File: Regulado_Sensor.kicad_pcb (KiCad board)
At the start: 2 copper layers, 57 parts

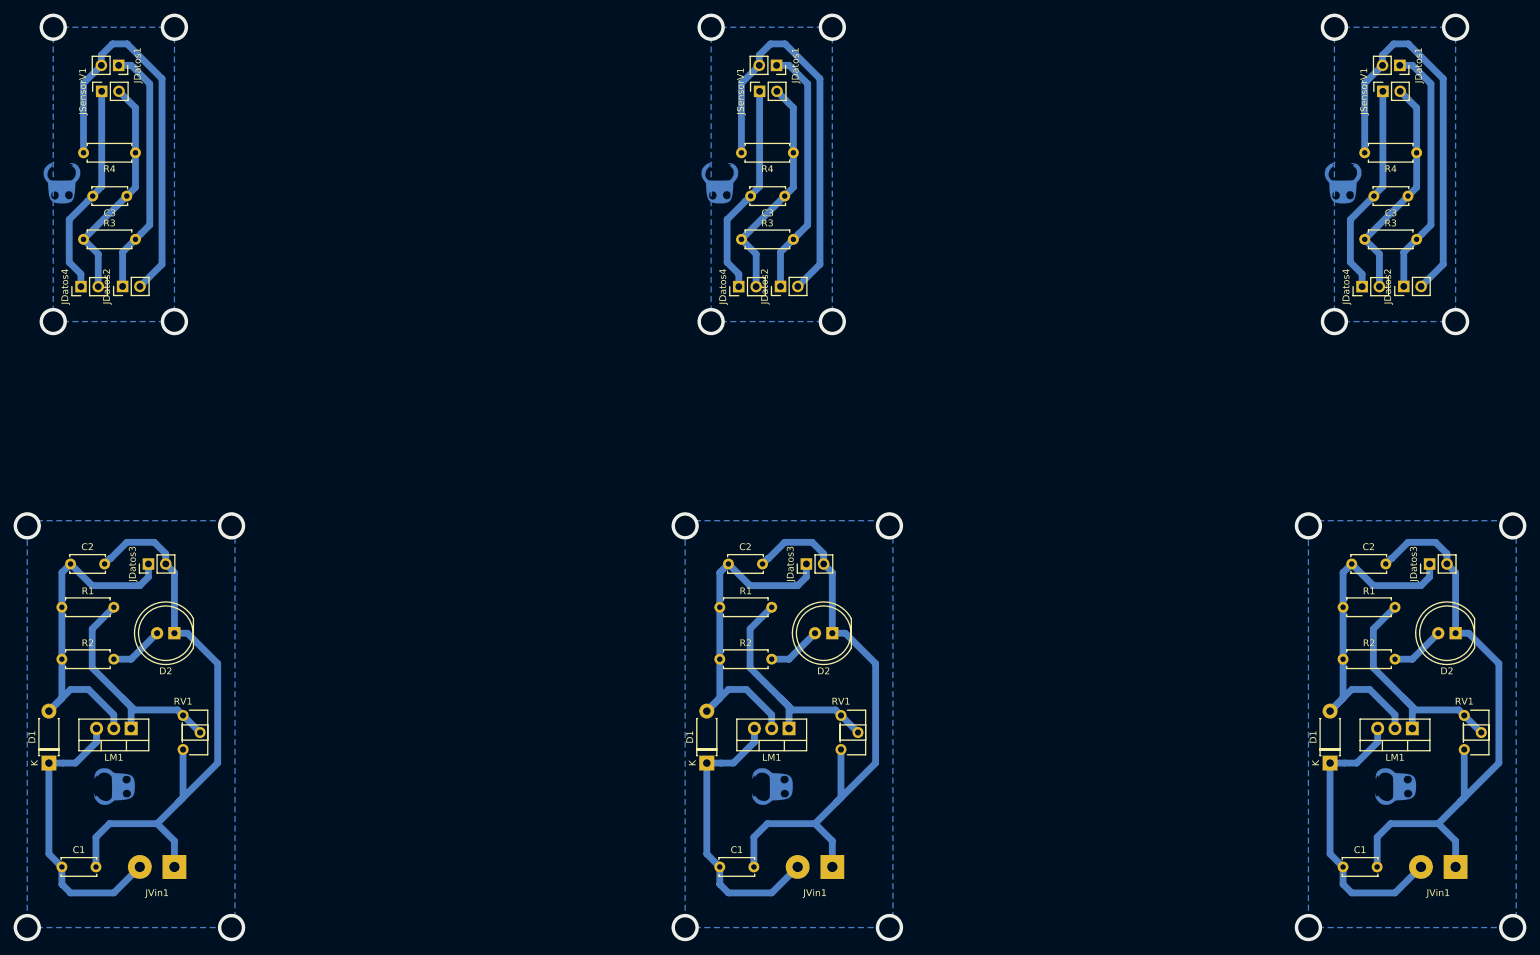
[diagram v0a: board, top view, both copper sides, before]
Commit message: Se arreglo un error en la placa de I2C
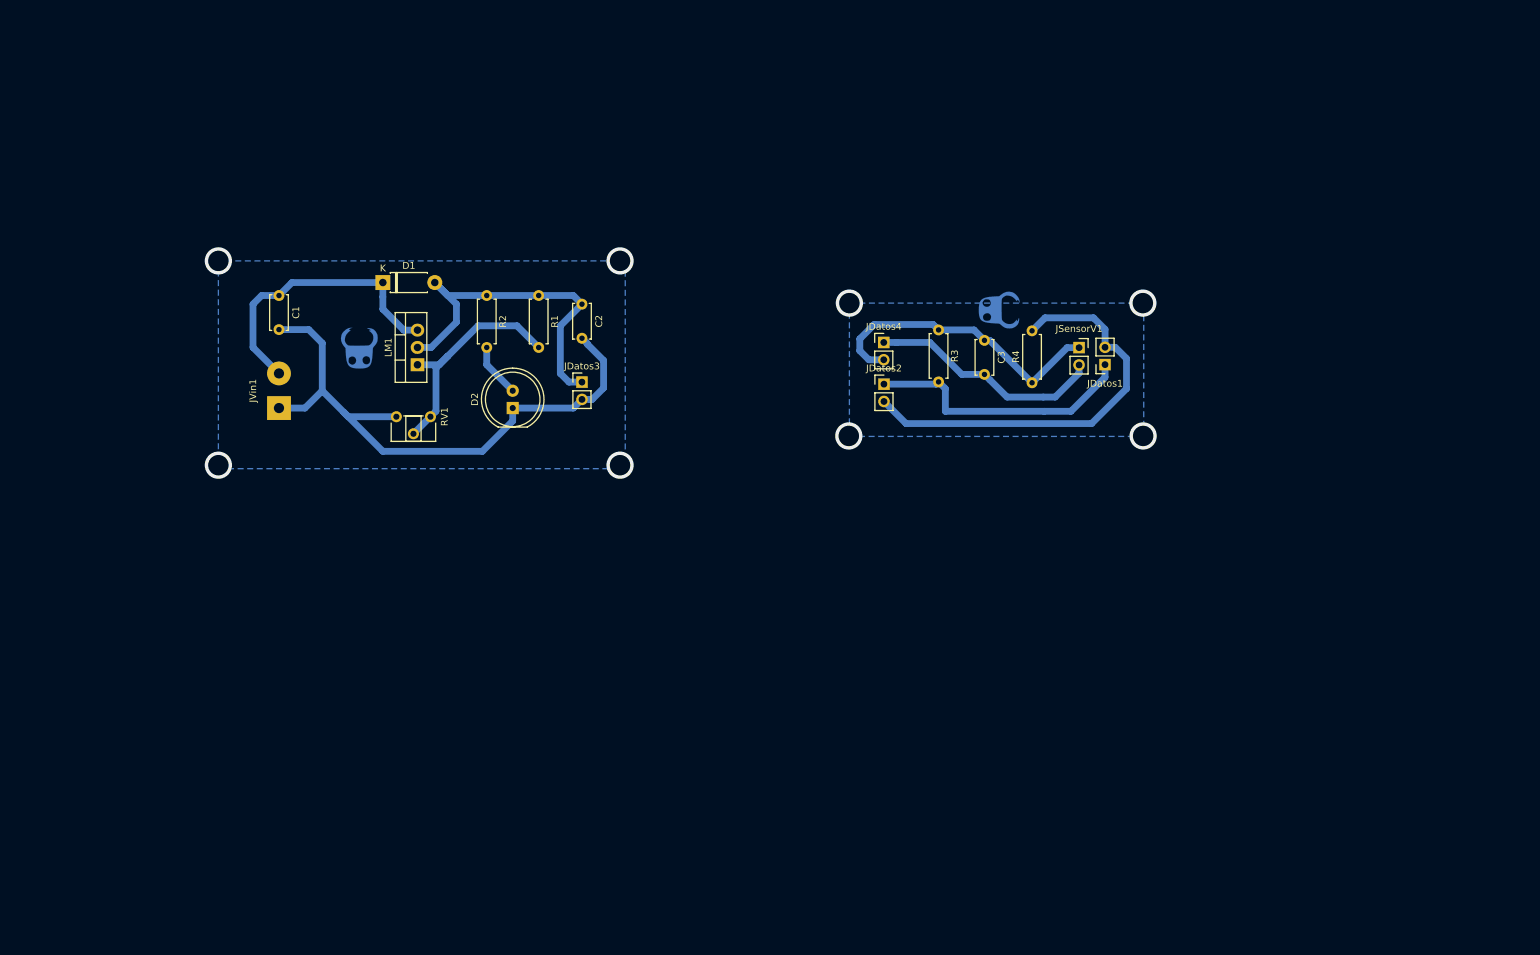
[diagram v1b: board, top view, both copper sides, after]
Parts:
- removed the ? at (231.9, 59.1)
- removed the ? at (239.6, 147.7)
- removed the ? at (140.5, 59.1)
- removed the ? at (148.2, 147.7)
- removed the C1 at (231.9, 159.5)
- removed the C1 at (140.5, 159.5)
- removed the C2 at (233.2, 115.0)
- removed the C2 at (141.7, 115.0)
- removed the C3 at (241.4, 61.0)
- removed the C3 at (150.0, 61.0)
- removed the D1 at (230.0, 144.2)
- removed the D1 at (138.6, 144.2)
- removed the D2 at (248.4, 125.2)
- removed the D2 at (157.0, 125.2)
- removed the JDatos1 at (240.2, 41.9)
- removed the JDatos1 at (148.8, 41.9)
- removed the JDatos2 at (240.8, 74.3)
- removed the JDatos2 at (149.4, 74.3)
- removed the JDatos3 at (244.6, 115.0)
- removed the JDatos3 at (153.2, 115.0)
- removed the JDatos4 at (234.7, 74.3)
- removed the JDatos4 at (143.3, 74.3)
- removed the JSensorV1 at (237.7, 45.7)
- removed the JSensorV1 at (146.3, 45.7)
- removed the JVin1 at (248.4, 159.5)
- removed the JVin1 at (157.0, 159.5)
- removed the LM1 at (242.1, 139.1)
- removed the LM1 at (150.6, 139.1)
- removed the R1 at (231.9, 121.4)
- removed the R1 at (140.5, 121.4)
- removed the R2 at (231.9, 129.0)
- removed the R2 at (140.5, 129.0)
- removed the R3 at (235.1, 67.4)
- removed the R3 at (143.6, 67.4)
- removed the R4 at (242.7, 54.7)
- removed the R4 at (151.3, 54.7)
- removed the RV1 at (249.7, 137.2)
- removed the RV1 at (158.2, 137.2)
- moved JDatos1 151.2 mm to (197.0, 85.8), turned to 180 degrees
- moved JSensorV1 148.2 mm to (193.2, 83.3), turned to 0 degrees
- moved ? 138.8 mm to (181.4, 77.7), turned to 270 degrees
- moved R4 135.8 mm to (186.3, 88.4), turned to 90 degrees
- moved C3 127.6 mm to (179.3, 82.2), turned to 270 degrees
- moved R3 126.1 mm to (172.6, 80.7), turned to 270 degrees
- moved JDatos4 118.1 mm to (164.5, 82.5), turned to 0 degrees
- moved JDatos2 112.6 mm to (164.5, 88.6), turned to 0 degrees
- moved C1 89.7 mm to (75.8, 75.6), turned to 270 degrees
- moved D1 85.9 mm to (91.0, 73.7), turned to 0 degrees
- moved C2 84.2 mm to (120.2, 76.9), turned to 270 degrees
- moved R1 83.6 mm to (113.9, 75.6), turned to 270 degrees
- moved R2 82.0 mm to (106.3, 75.6), turned to 270 degrees
- moved ? 73.7 mm to (87.6, 83.3), turned to 0 degrees
- moved JVin1 69.0 mm to (75.8, 92.1), turned to 90 degrees
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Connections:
- JSensorV1 pad 1: Net-(C3-Pad2) -> Net-(C3-Pad1)
- JSensorV1 pad 2: Net-(C3-Pad1) -> Net-(C3-Pad2)
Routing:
- net (no net): track 774.6 -> 0.00 mm, vias 24 -> 8
- net Net-(C3-Pad1): track 33.7 -> 44.5 mm
- net Net-(C3-Pad2): track 31.3 -> 34.6 mm
- net Net-(JDatos1-Pad2): track 58.9 -> 62.1 mm
- net Net-(JDatos1-Pad1): track 37.6 -> 40.2 mm
- added copper zone on B.Cu, net Net-(C3-Pad2)
- removed copper zone on B.Cu, net (none)
- removed copper zone on B.Cu, net Net-(C3-Pad1)
